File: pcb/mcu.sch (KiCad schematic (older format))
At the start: 22 parts, among them J2 CONN_INTEGRALSTICK_MCU_DEVICE, U1 STM32F777NIH6‎, U10 DSC6083MI2A-032K768, U2 XC7A50T-1FTG256C, U6 S25FL064LABNFI011‎

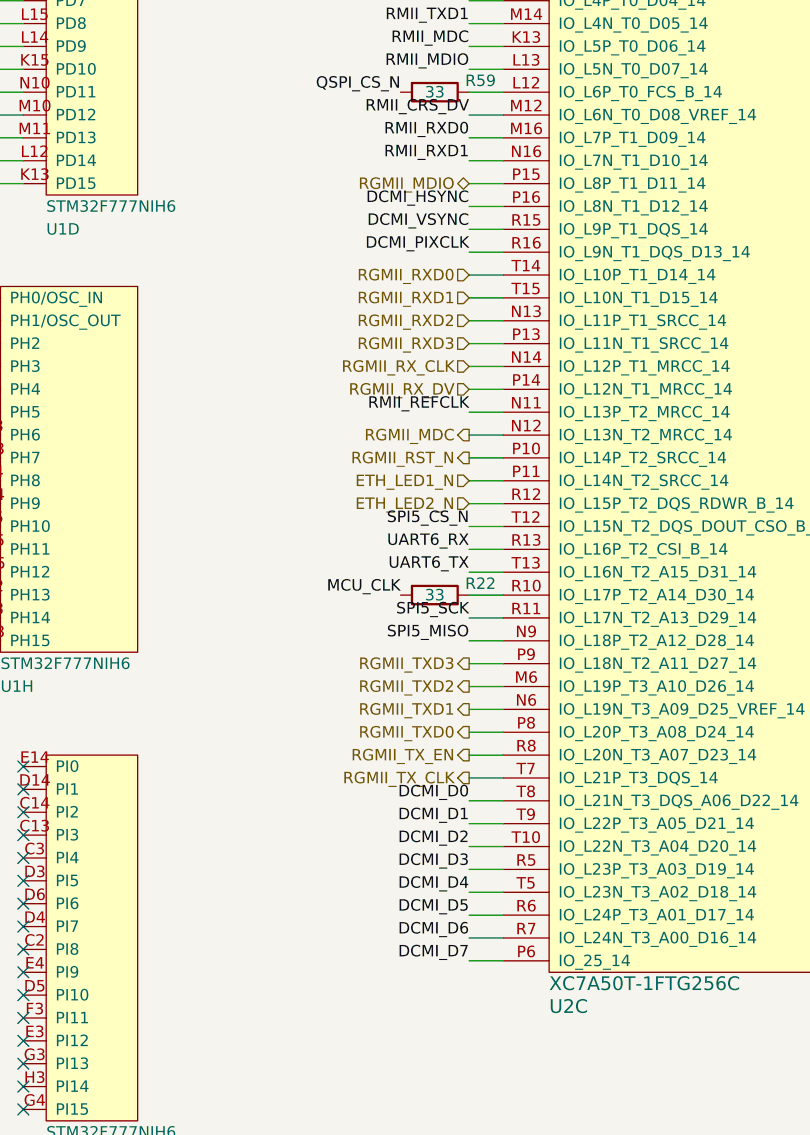
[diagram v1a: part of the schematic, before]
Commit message: Continued FPGA layout. Fanned out most signals going to MCU but pin assignments aren't final.
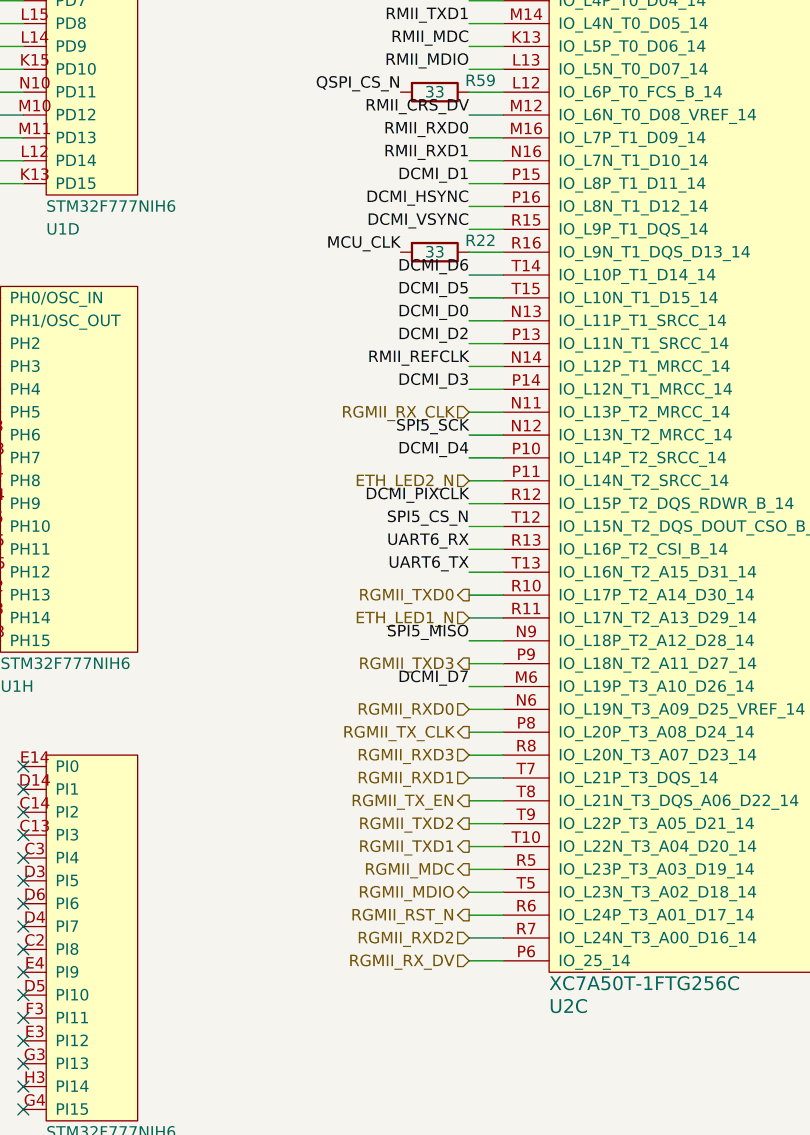
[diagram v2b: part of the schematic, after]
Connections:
- net DCMI_D0: now also U2.N13 (IO_L11P_T1_SRCC_14); no longer U2.T8 (IO_L21N_T3_DQS_A06_D22_14)
- net DCMI_D1: now also U2.P15 (IO_L8P_T1_D11_14); no longer U2.T9 (IO_L22P_T3_A05_D21_14)
- net DCMI_D2: now also U2.P13 (IO_L11N_T1_SRCC_14); no longer U2.T10 (IO_L22N_T3_A04_D20_14)
- net DCMI_D3: now also U2.P14 (IO_L12N_T1_MRCC_14); no longer U2.R5 (IO_L23P_T3_A03_D19_14)
- net DCMI_D4: now also U2.P10 (IO_L14P_T2_SRCC_14); no longer U2.T5 (IO_L23N_T3_A02_D18_14)
- net DCMI_D5: now also U2.T15 (IO_L10N_T1_D15_14); no longer U2.R6 (IO_L24P_T3_A01_D17_14)
- net DCMI_D6: now also U2.T14 (IO_L10P_T1_D14_14); no longer U2.R7 (IO_L24N_T3_A00_D16_14)
- net DCMI_D7: now also U2.M6 (IO_L19P_T3_A10_D26_14); no longer U2.P6 (IO_25_14)
- net DCMI_PIXCLK: now also U2.R12 (IO_L15P_T2_DQS_RDWR_B_14); no longer U2.R16 (IO_L9N_T1_DQS_D13_14)
- net ETH_LED1_N: now also U2.R11 (IO_L17N_T2_A13_D29_14); no longer U2.P11 (IO_L14N_T2_SRCC_14)
- net ETH_LED2_N: now also U2.P11 (IO_L14N_T2_SRCC_14); no longer U2.R12 (IO_L15P_T2_DQS_RDWR_B_14)
- net RGMII_MDC: now also U2.R5 (IO_L23P_T3_A03_D19_14); no longer U2.N12 (IO_L13N_T2_MRCC_14)
- net RGMII_MDIO: now also U2.T5 (IO_L23N_T3_A02_D18_14); no longer U2.P15 (IO_L8P_T1_D11_14)
- net RGMII_RST_N: now also U2.R6 (IO_L24P_T3_A01_D17_14); no longer U2.P10 (IO_L14P_T2_SRCC_14)
- net RGMII_RXD0: now also U2.N6 (IO_L19N_T3_A09_D25_VREF_14); no longer U2.T14 (IO_L10P_T1_D14_14)
- net RGMII_RXD1: now also U2.T7 (IO_L21P_T3_DQS_14); no longer U2.T15 (IO_L10N_T1_D15_14)
- net RGMII_RXD2: now also U2.R7 (IO_L24N_T3_A00_D16_14); no longer U2.N13 (IO_L11P_T1_SRCC_14)
- net RGMII_RXD3: now also U2.R8 (IO_L20N_T3_A07_D23_14); no longer U2.P13 (IO_L11N_T1_SRCC_14)
- net RGMII_RX_CLK: now also U2.N11 (IO_L13P_T2_MRCC_14); no longer U2.N14 (IO_L12P_T1_MRCC_14)
- net RGMII_RX_DV: now also U2.P6 (IO_25_14); no longer U2.P14 (IO_L12N_T1_MRCC_14)
- net RGMII_TXD0: now also U2.R10 (IO_L17P_T2_A14_D30_14); no longer U2.P8 (IO_L20P_T3_A08_D24_14)
- net RGMII_TXD1: now also U2.T10 (IO_L22N_T3_A04_D20_14); no longer U2.N6 (IO_L19N_T3_A09_D25_VREF_14)
- net RGMII_TXD2: now also U2.T9 (IO_L22P_T3_A05_D21_14); no longer U2.M6 (IO_L19P_T3_A10_D26_14)
- net RGMII_TX_CLK: now also U2.P8 (IO_L20P_T3_A08_D24_14); no longer U2.T7 (IO_L21P_T3_DQS_14)
- net RGMII_TX_EN: now also U2.T8 (IO_L21N_T3_DQS_A06_D22_14); no longer U2.R8 (IO_L20N_T3_A07_D23_14)
- net RMII_REFCLK: now also U2.N14 (IO_L12P_T1_MRCC_14); no longer U2.N11 (IO_L13P_T2_MRCC_14)
- net SPI5_SCK: now also U2.N12 (IO_L13N_T2_MRCC_14); no longer U2.R11 (IO_L17N_T2_A13_D29_14)
- net at R22.1: now also U2.R16 (IO_L9N_T1_DQS_D13_14); no longer U2.R10 (IO_L17P_T2_A14_D30_14)
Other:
- moved on the sheet: R22
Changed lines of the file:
@@
 Sheet 8 8
 Title "INTEGRALSTICK Compute Module"
-Date "2018-11-13"
+Date "2018-11-14"
 Rev "0.1"
 Comp "Andrew D. Zonenberg"
@@
 Text Label 13950 1650 2    50   ~ 0
 RMII_TXD1
-Text Label 13950 5550 2    50   ~ 0
+Text Label 13950 2850 2    50   ~ 0
 DCMI_D5
 Text Label 13950 2550 2    50   ~ 0
 DCMI_VSYNC
-Text Label 13950 5650 2    50   ~ 0
+Text Label 13950 2750 2    50   ~ 0
 DCMI_D6
-Text Label 13950 5750 2    50   ~ 0
+Text Label 13950 4550 2    50   ~ 0
 DCMI_D7
 Text Label 13950 2150 2    50   ~ 0
@@
 Text Label 13950 2250 2    50   ~ 0
 RMII_RXD1
-Text Label 13950 5050 2    50   ~ 0
+Text Label 13950 2950 2    50   ~ 0
 DCMI_D0
-Text Label 13950 5150 2    50   ~ 0
+Text Label 13950 2350 2    50   ~ 0
 DCMI_D1
-Text Label 13950 5250 2    50   ~ 0
+Text Label 13950 3050 2    50   ~ 0
 DCMI_D2
-Text Label 13950 5350 2    50   ~ 0
+Text Label 13950 3250 2    50   ~ 0
 DCMI_D3
-Text Label 13950 5450 2    50   ~ 0
+Text Label 13950 3550 2    50   ~ 0
 DCMI_D4
-Text Label 13950 3350 2    50   ~ 0
+Text Label 13950 3150 2    50   ~ 0
 RMII_REFCLK
 Text Label 13950 1850 2    50   ~ 0
@@
 Text Label 13950 2450 2    50   ~ 0
 DCMI_HSYNC
-Text Label 13950 2650 2    50   ~ 0
+Text Label 13950 3750 2    50   ~ 0
 DCMI_PIXCLK
 $Comp
@@
 Wire Wire Line
 	14100 5750 13950 5750
-Text HLabel 13950 4950 0    50   Output ~ 0
+Text HLabel 13950 4750 0    50   Output ~ 0
 RGMII_TX_CLK
-Text HLabel 13950 4850 0    50   Output ~ 0
+Text HLabel 13950 5050 0    50   Output ~ 0
 RGMII_TX_EN
-Text HLabel 13950 4750 0    50   Output ~ 0
+Text HLabel 13950 4150 0    50   Output ~ 0
 RGMII_TXD0
-Text HLabel 13950 4650 0    50   Output ~ 0
+Text HLabel 13950 5250 0    50   Output ~ 0
 RGMII_TXD1
-Text HLabel 13950 4550 0    50   Output ~ 0
+Text HLabel 13950 5150 0    50   Output ~ 0
 RGMII_TXD2
 Text HLabel 13950 4450 0    50   Output ~ 0
@@
 Wire Wire Line
 	14100 4950 13950 4950
-Text HLabel 13950 3150 0    50   Input ~ 0
+Text HLabel 13950 3350 0    50   Input ~ 0
 RGMII_RX_CLK
-Text HLabel 13950 3250 0    50   Input ~ 0
+Text HLabel 13950 5750 0    50   Input ~ 0
 RGMII_RX_DV
-Text HLabel 13950 2750 0    50   Input ~ 0
+Text HLabel 13950 4650 0    50   Input ~ 0
 RGMII_RXD0
-Text HLabel 13950 2850 0    50   Input ~ 0
+Text HLabel 13950 4950 0    50   Input ~ 0
 RGMII_RXD1
-Text HLabel 13950 2950 0    50   Input ~ 0
+Text HLabel 13950 5650 0    50   Input ~ 0
 RGMII_RXD2
-Text HLabel 13950 3050 0    50   Input ~ 0
+Text HLabel 13950 4850 0    50   Input ~ 0
 RGMII_RXD3
 Wire Wire Line
@@
 Wire Wire Line
 	14100 3250 13950 3250
-Text HLabel 13950 2350 0    50   BiDi ~ 0
+Text HLabel 13950 5450 0    50   BiDi ~ 0
 RGMII_MDIO
-Text HLabel 13950 3450 0    50   Output ~ 0
+Text HLabel 13950 5350 0    50   Output ~ 0
 RGMII_MDC
 Wire Wire Line
@@
 Wire Wire Line
 	14100 2350 13950 2350
-Text HLabel 13950 3550 0    50   Output ~ 0
+Text HLabel 13950 5550 0    50   Output ~ 0
 RGMII_RST_N
 Wire Wire Line
@@
 Wire Wire Line
 	13950 3750 14100 3750
+Text HLabel 13950 4250 0    50   Input ~ 0
+ETH_LED1_N
 Text HLabel 13950 3650 0    50   Input ~ 0
-ETH_LED1_N
-Text HLabel 13950 3750 0    50   Input ~ 0
 ETH_LED2_N
 Text HLabel 13200 1350 0    50   Input ~ 0
@@
 L device:R R22
 U 1 1 5BEE00F4
-P 13800 4150
-F 0 "R22" V 13750 4350 50  0000 C CNN
-F 1 "33" V 13800 4150 50  0000 C CNN
-F 2 "azonenberg_pcb:EIA_0402_RES_NOSILK" V 13730 4150 50  0001 C CNN
-F 3 "" H 13800 4150 50  0001 C CNN
-	1    13800 4150
+P 13800 2650
+F 0 "R22" V 13750 2850 50  0000 C CNN
+F 1 "33" V 13800 2650 50  0000 C CNN
+F 2 "azonenberg_pcb:EIA_0402_RES_NOSILK" V 13730 2650 50  0001 C CNN
+F 3 "" H 13800 2650 50  0001 C CNN
+	1    13800 2650
 	0    1    1    0
 $EndComp
-Text Label 13650 4150 2    50   ~ 0
+Text Label 13650 2650 2    50   ~ 0
 MCU_CLK
 Text Label 11650 2850 2    50   ~ 0
@@
 Text Label 13950 3850 2    50   ~ 0
 SPI5_CS_N
-Text Label 13950 4250 2    50   ~ 0
+Text Label 13950 3450 2    50   ~ 0
 SPI5_SCK
 Text Label 13950 4350 2    50   ~ 0

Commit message: Initial STM32 fanout
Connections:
- net DCMI_D3: now also U2.P16 (IO_L8N_T1_D12_14); no longer U2.P14 (IO_L12N_T1_MRCC_14)
- net DCMI_HSYNC: now also U2.R12 (IO_L15P_T2_DQS_RDWR_B_14); no longer U2.P16 (IO_L8N_T1_D12_14)
- net DCMI_PIXCLK: now also U2.P14 (IO_L12N_T1_MRCC_14); no longer U2.R12 (IO_L15P_T2_DQS_RDWR_B_14)
- net RMII_CRS_DV: now also U2.L14 (IO_L4P_T0_D04_14); no longer U2.M12 (IO_L6N_T0_D08_VREF_14)
- net RMII_MDC: now also U2.N16 (IO_L7N_T1_D10_14); no longer U2.K13 (IO_L5P_T0_D06_14)
- net RMII_MDIO: now also U2.K13 (IO_L5P_T0_D06_14); no longer U2.L13 (IO_L5N_T0_D07_14)
- net RMII_REFCLK: now also U2.K12 (IO_0_14); no longer U2.N14 (IO_L12P_T1_MRCC_14)
- net RMII_RXD0: now also U2.L13 (IO_L5N_T0_D07_14); no longer U2.M16 (IO_L7P_T1_D09_14)
- net RMII_RXD1: now also U2.M14 (IO_L4N_T0_D05_14); no longer U2.N16 (IO_L7N_T1_D10_14)
- net RMII_TXD0: now also U2.M12 (IO_L6N_T0_D08_VREF_14); no longer U2.L14 (IO_L4P_T0_D04_14)
- net RMII_TXD1: now also U2.M16 (IO_L7P_T1_D09_14); no longer U2.M14 (IO_L4N_T0_D05_14)
- net SPI5_MOSI: now also U2.N14 (IO_L12P_T1_MRCC_14); no longer U2.K12 (IO_0_14)
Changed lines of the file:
@@
 Sheet 8 8
 Title "INTEGRALSTICK Compute Module"
-Date "2018-11-19"
+Date "2018-11-20"
 Rev "0.1"
 Comp "Andrew D. Zonenberg"
@@
 Text Label 13950 1450 2    50   ~ 0
 RMII_TX_EN
-Text Label 13950 1550 2    50   ~ 0
+Text Label 13950 2050 2    50   ~ 0
 RMII_TXD0
-Text Label 13950 1650 2    50   ~ 0
+Text Label 13950 2150 2    50   ~ 0
 RMII_TXD1
 Text Label 13950 2850 2    50   ~ 0
@@
 Text Label 13950 4550 2    50   ~ 0
 DCMI_D7
-Text Label 13950 2150 2    50   ~ 0
+Text Label 13950 1850 2    50   ~ 0
 RMII_RXD0
-Text Label 13950 2250 2    50   ~ 0
+Text Label 13950 1650 2    50   ~ 0
 RMII_RXD1
 Text Label 13950 2950 2    50   ~ 0
@@
 Text Label 13950 3050 2    50   ~ 0
 DCMI_D2
-Text Label 13950 3250 2    50   ~ 0
+Text Label 13950 2450 2    50   ~ 0
 DCMI_D3
 Text Label 13950 3550 2    50   ~ 0
 DCMI_D4
-Text Label 13950 3150 2    50   ~ 0
+Text Label 13950 850  2    50   ~ 0
 RMII_REFCLK
-Text Label 13950 1850 2    50   ~ 0
+Text Label 13950 1750 2    50   ~ 0
 RMII_MDIO
-Text Label 13950 2050 2    50   ~ 0
+Text Label 13950 1550 2    50   ~ 0
 RMII_CRS_DV
-Text Label 13950 2450 2    50   ~ 0
+Text Label 13950 3750 2    50   ~ 0
 DCMI_HSYNC
-Text Label 13950 3750 2    50   ~ 0
+Text Label 13950 3250 2    50   ~ 0
 DCMI_PIXCLK
 $Comp
@@
 Wire Wire Line
 	8300 1250 8500 1250
-Text Label 13950 1750 2    50   ~ 0
+Text Label 13950 2250 2    50   ~ 0
 RMII_MDC
 Wire Wire Line
@@
 Text Label 6150 3950 2    50   ~ 0
 SPI5_MOSI
-Text Label 13950 850  2    50   ~ 0
+Text Label 13950 3150 2    50   ~ 0
 SPI5_MOSI
 Wire Wire Line

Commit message: Finished initial routing
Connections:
- net DCMI_D0: now also U2.T14 (IO_L10P_T1_D14_14); no longer U2.N13 (IO_L11P_T1_SRCC_14)
- net DCMI_D1: now also U2.R13 (IO_L16P_T2_CSI_B_14); no longer U2.P15 (IO_L8P_T1_D11_14)
- net DCMI_D3: now also U2.T13 (IO_L16N_T2_A15_D31_14); no longer U2.P16 (IO_L8N_T1_D12_14)
- net DCMI_D4: now also U2.N12 (IO_L13N_T2_MRCC_14); no longer U2.P10 (IO_L14P_T2_SRCC_14)
- net DCMI_D5: now also U2.R12 (IO_L15P_T2_DQS_RDWR_B_14); no longer U2.T15 (IO_L10N_T1_D15_14)
- net DCMI_D6: now also U2.M6 (IO_L19P_T3_A10_D26_14); no longer U2.T14 (IO_L10P_T1_D14_14)
- net DCMI_D7: now also U2.M14 (IO_L4N_T0_D05_14); no longer U2.M6 (IO_L19P_T3_A10_D26_14)
- net DCMI_HSYNC: now also U2.P16 (IO_L8N_T1_D12_14); no longer U2.R12 (IO_L15P_T2_DQS_RDWR_B_14)
- net DCMI_PIXCLK: now also U2.L14 (IO_L4P_T0_D04_14); no longer U2.P14 (IO_L12N_T1_MRCC_14)
- net DCMI_VSYNC: now also U2.T12 (IO_L15N_T2_DQS_DOUT_CSO_B_14); no longer U2.R15 (IO_L9P_T1_DQS_14)
- net RMII_CRS_DV: now also U2.P14 (IO_L12N_T1_MRCC_14); no longer U2.L14 (IO_L4P_T0_D04_14)
- net RMII_MDC: now also U2.N14 (IO_L12P_T1_MRCC_14); no longer U2.N16 (IO_L7N_T1_D10_14)
- net RMII_RXD0: now also U2.R16 (IO_L9N_T1_DQS_D13_14); no longer U2.L13 (IO_L5N_T0_D07_14)
- net RMII_RXD1: now also U2.R15 (IO_L9P_T1_DQS_14); no longer U2.M14 (IO_L4N_T0_D05_14)
- net RMII_TXD0: now also U2.P15 (IO_L8P_T1_D11_14); no longer U2.M12 (IO_L6N_T0_D08_VREF_14)
- net RMII_TXD1: now also U2.T15 (IO_L10N_T1_D15_14); no longer U2.M16 (IO_L7P_T1_D09_14)
- net SPI5_CS_N: now also U2.N16 (IO_L7N_T1_D10_14); no longer U2.T12 (IO_L15N_T2_DQS_DOUT_CSO_B_14)
- net SPI5_MISO: now also U2.P10 (IO_L14P_T2_SRCC_14); no longer U2.N9 (IO_L18P_T2_A12_D28_14)
- net SPI5_MOSI: now also U2.M12 (IO_L6N_T0_D08_VREF_14); no longer U2.N14 (IO_L12P_T1_MRCC_14)
- net SPI5_SCK: now also U2.M16 (IO_L7P_T1_D09_14); no longer U2.N12 (IO_L13N_T2_MRCC_14)
- net UART6_RX: now also U2.L13 (IO_L5N_T0_D07_14); no longer U2.R13 (IO_L16P_T2_CSI_B_14)
- net UART6_TX: now also U2.N9 (IO_L18P_T2_A12_D28_14); no longer U2.T13 (IO_L16N_T2_A15_D31_14)
- net at R22.1: now also U2.N13 (IO_L11P_T1_SRCC_14); no longer U2.R16 (IO_L9N_T1_DQS_D13_14)
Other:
- moved on the sheet: R22
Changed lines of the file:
@@
 Sheet 8 8
 Title "INTEGRALSTICK Compute Module"
-Date "2018-11-20"
+Date "2018-11-23"
 Rev "0.1"
 Comp "Andrew D. Zonenberg"
@@
 Text Label 13950 1450 2    50   ~ 0
 RMII_TX_EN
-Text Label 13950 2050 2    50   ~ 0
+Text Label 13950 2350 2    50   ~ 0
 RMII_TXD0
-Text Label 13950 2150 2    50   ~ 0
+Text Label 13950 2850 2    50   ~ 0
 RMII_TXD1
-Text Label 13950 2850 2    50   ~ 0
+Text Label 13950 3750 2    50   ~ 0
 DCMI_D5
+Text Label 13950 3850 2    50   ~ 0
+DCMI_VSYNC
+Text Label 13950 4550 2    50   ~ 0
+DCMI_D6
+Text Label 13950 1650 2    50   ~ 0
+DCMI_D7
+Text Label 13950 2650 2    50   ~ 0
+RMII_RXD0
 Text Label 13950 2550 2    50   ~ 0
-DCMI_VSYNC
+RMII_RXD1
 Text Label 13950 2750 2    50   ~ 0
-DCMI_D6
-Text Label 13950 4550 2    50   ~ 0
-DCMI_D7
-Text Label 13950 1850 2    50   ~ 0
-RMII_RXD0
-Text Label 13950 1650 2    50   ~ 0
-RMII_RXD1
-Text Label 13950 2950 2    50   ~ 0
 DCMI_D0
-Text Label 13950 2350 2    50   ~ 0
+Text Label 13950 3950 2    50   ~ 0
 DCMI_D1
 Text Label 13950 3050 2    50   ~ 0
 DCMI_D2
-Text Label 13950 2450 2    50   ~ 0
+Text Label 13950 4050 2    50   ~ 0
 DCMI_D3
-Text Label 13950 3550 2    50   ~ 0
+Text Label 13950 3450 2    50   ~ 0
 DCMI_D4
 Text Label 13950 850  2    50   ~ 0
@@
 Text Label 13950 1750 2    50   ~ 0
 RMII_MDIO
+Text Label 13950 3250 2    50   ~ 0
+RMII_CRS_DV
+Text Label 13950 2450 2    50   ~ 0
+DCMI_HSYNC
 Text Label 13950 1550 2    50   ~ 0
-RMII_CRS_DV
-Text Label 13950 3750 2    50   ~ 0
-DCMI_HSYNC
-Text Label 13950 3250 2    50   ~ 0
 DCMI_PIXCLK
 $Comp
@@
 Wire Wire Line
 	8300 1250 8500 1250
-Text Label 13950 2250 2    50   ~ 0
+Text Label 13950 3150 2    50   ~ 0
 RMII_MDC
 Wire Wire Line
@@
 L device:R R22
 U 1 1 5BEE00F4
-P 13800 2650
-F 0 "R22" V 13750 2850 50  0000 C CNN
-F 1 "33" V 13800 2650 50  0000 C CNN
-F 2 "azonenberg_pcb:EIA_0402_RES_NOSILK" V 13730 2650 50  0001 C CNN
-F 3 "" H 13800 2650 50  0001 C CNN
-	1    13800 2650
+P 13800 2950
+F 0 "R22" V 13750 3150 50  0000 C CNN
+F 1 "33" V 13800 2950 50  0000 C CNN
+F 2 "azonenberg_pcb:EIA_0402_RES_NOSILK" V 13730 2950 50  0001 C CNN
+F 3 "" H 13800 2950 50  0001 C CNN
+	1    13800 2950
 	0    1    1    0
 $EndComp
-Text Label 13650 2650 2    50   ~ 0
+Text Label 13650 2950 2    50   ~ 0
 MCU_CLK
 Text Label 11650 2850 2    50   ~ 0
@@
 Text Label 8850 4250 2    50   ~ 0
 UART6_TX
-Text Label 13950 3950 2    50   ~ 0
+Text Label 13950 1850 2    50   ~ 0
 UART6_RX
-Text Label 13950 4050 2    50   ~ 0
+Text Label 13950 4350 2    50   ~ 0
 UART6_TX
 Wire Wire Line
@@
 Text Label 6150 3950 2    50   ~ 0
 SPI5_MOSI
-Text Label 13950 3150 2    50   ~ 0
+Text Label 13950 2050 2    50   ~ 0
 SPI5_MOSI
 Wire Wire Line
 	14100 850  13950 850
-Text Label 13950 3850 2    50   ~ 0
+Text Label 13950 2250 2    50   ~ 0
 SPI5_CS_N
-Text Label 13950 3450 2    50   ~ 0
+Text Label 13950 2150 2    50   ~ 0
 SPI5_SCK
-Text Label 13950 4350 2    50   ~ 0
+Text Label 13950 3550 2    50   ~ 0
 SPI5_MISO
 Wire Wire Line
